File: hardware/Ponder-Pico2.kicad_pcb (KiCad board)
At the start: 2 copper layers, 40 x 50 mm, 136 parts, among them J1 USB_C_Receptacle_USB2.0, J10 2.54 SKT, J11 2.54 HDR, J12 1.27 HDR, J13 1.27 HDR, J14 1.27 HDR, J15 1.27 HDR, J2 2.54 HDR, J3 2.54 HDR, J4 2.54 HDR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

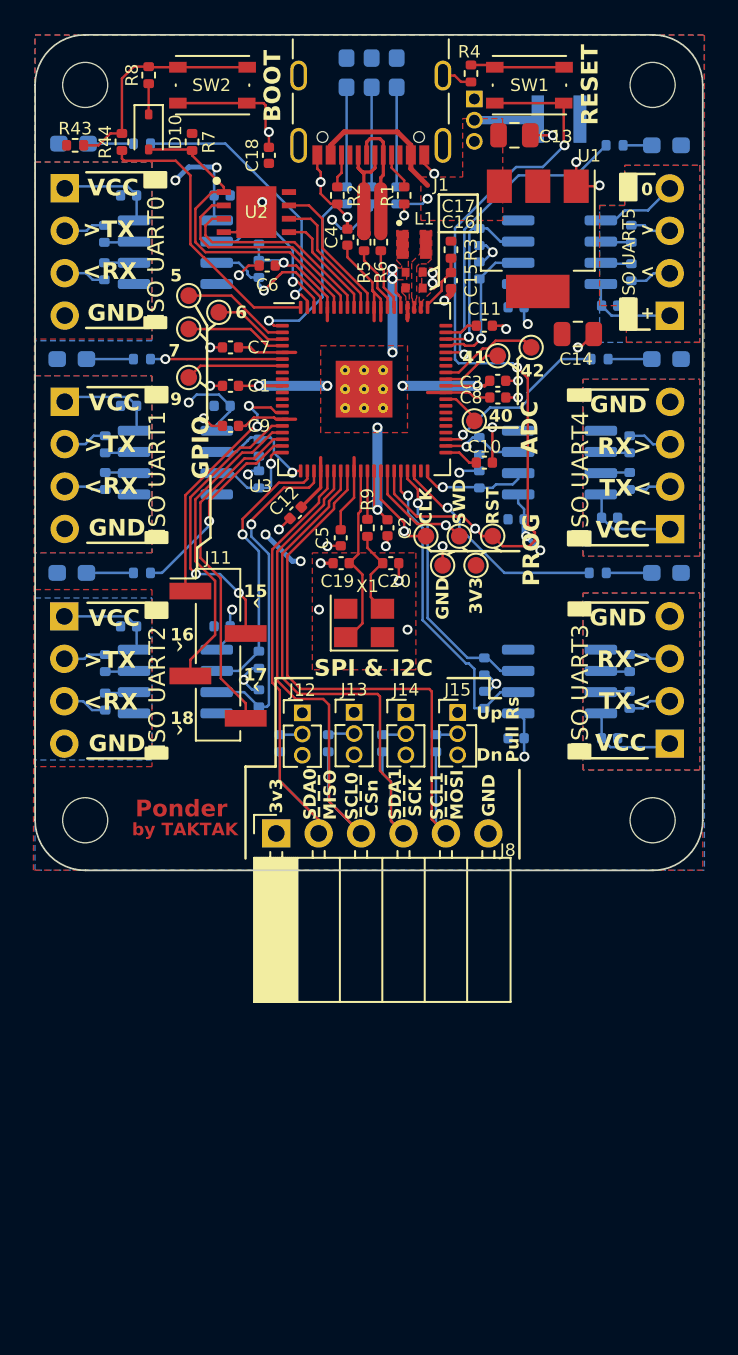
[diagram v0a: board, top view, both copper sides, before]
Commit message: Adding start of Pico 2 variant for Ponder
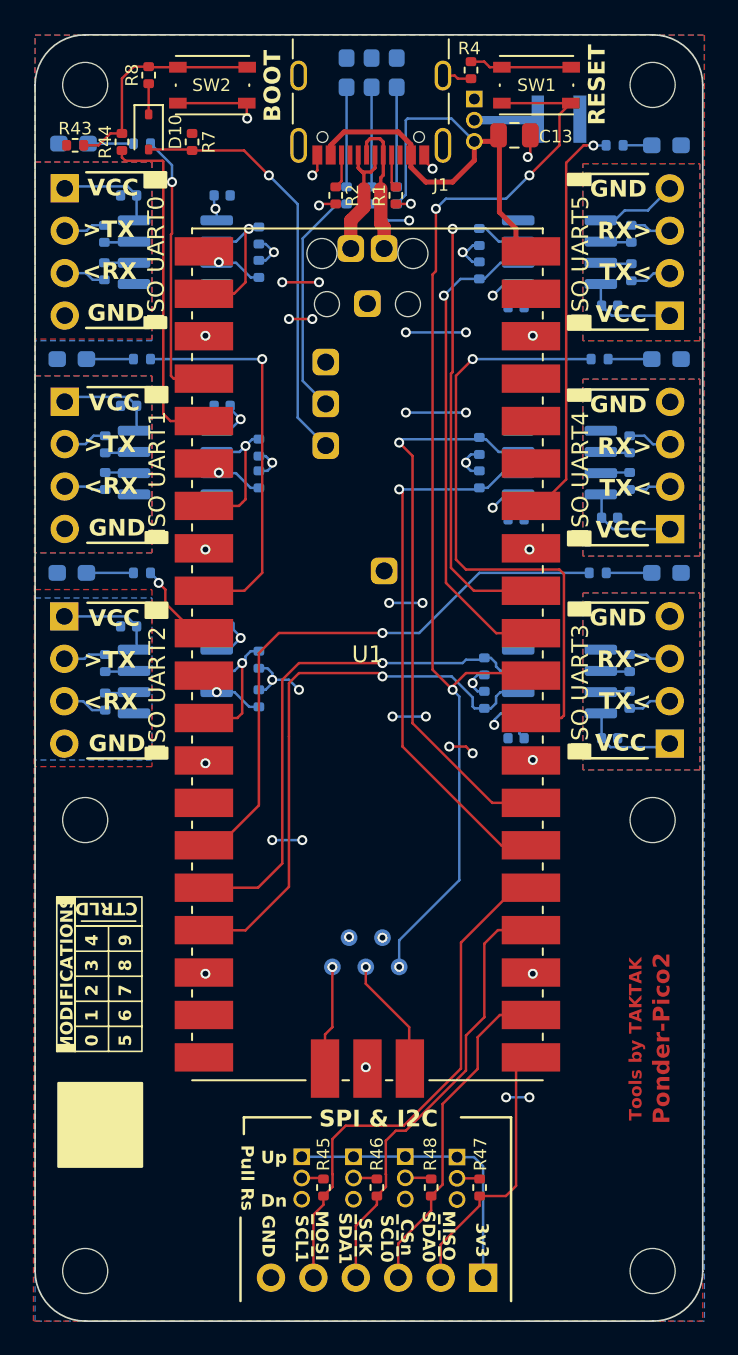
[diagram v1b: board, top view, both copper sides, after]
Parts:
- removed C1, C10, C11, C12, C18, C3, C4, C5, C6, C7, C8, C9: 100n, Capacitor_SMD:C_0402_1005Metric
- removed C14: 10u, Capacitor_SMD:C_0805_2012Metric
- removed C15, C2: 4.7u, Capacitor_SMD:C_0402_1005Metric
- removed C16, C17: 4.7u, Ponder:C_0402_1005Metric_small_pads
- removed C19, C20: 15p, Capacitor_SMD:C_0402_1005Metric
- removed J11: 2.54 HDR, Connector_PinHeader_2.54mm:PinHeader_1x04_P2.54mm_Vertical_SMD_Pin1Left
- removed L1: 3.3u, Ponder:L_pol_2016
- removed R3: 33, Resistor_SMD:R_0402_1005Metric
- removed R5, R6: 27, Resistor_SMD:R_0402_1005Metric
- removed R9: 1k, Resistor_SMD:R_0402_1005Metric
- removed TP10, TP11, TP12, TP6, TP7, TP8, TP9: TestPoint, TestPoint:TestPoint_Pad_D1.0mm
- removed U2: W25Q64JVXGIQ_TR, Ponder:SON80P400X400X50-9N
- removed U3: RP2350_80QFN, Ponder:RP2350-QFN-80-1EP_10x10_P0.4mm_EP3.4x3.4mm_ThermalVias
- removed X1: ABM8-272-T3, Crystal:Crystal_SMD_3225-4Pin_3.2x2.5mm
- added H5: MountingHole, MountingHole:MountingHole_2.7mm_M2.5, F.Cu at (123.6, 147.0)
- added H6: MountingHole, MountingHole:MountingHole_2.7mm_M2.5, F.Cu at (157.6, 147.0)
- G1, R45, R46, R47, R48: moved to F.Cu
- J12, J13, J14, J15, J8, TP1, TP2, TP3, TP4, TP5: moved to B.Cu
- U1: value NCP1117-3.3_SOT223 -> ~; footprint Package_TO_SOT_SMD:SOT-223-3_TabPin2 -> Ponder:RaspberryPi-Pico-SMD-TP
- moved U1 54.5 mm to (130.0, 135.6), turned to 0 degrees
- moved J8 29.3 mm to (147.4, 147.4)
- moved R47 29.2 mm to (147.2, 142.0)
- moved J15 28.2 mm to (136.6, 140.2), turned to 180 degrees
- moved J12 28.2 mm to (145.9, 140.2), turned to 180 degrees
- moved R45 27.4 mm to (137.9, 142.0)
- moved R48 27.3 mm to (144.3, 142.0)
- moved G1 26.9 mm to (125.0, 129.2), turned to 90 degrees
- moved J14 26.8 mm to (139.7, 140.2), turned to 180 degrees
- moved J13 26.8 mm to (142.8, 140.2), turned to 180 degrees
- moved R46 26.6 mm to (141.1, 142.0)
- moved TP1 26.4 mm to (138.4, 128.8)
- moved TP2 26.4 mm to (140.4, 128.8)
- moved TP5 26.4 mm to (142.4, 128.8)
- moved TP3 23.0 mm to (139.4, 127.0)
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- renumbered R25 to locked
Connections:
- D10 pad 2: /QSPI_SS -> /BOOTSEL
- J8 pad 2: /RP_SPI1-MISO_I2C0-SDA -> /RP_SPI0-MISO_I2C0-SDA
- J8 pad 3: /RP_SPI1-CSn_I2C0-SCL -> /RP_SPI0-CSn_I2C0-SCL
- J8 pad 4: /RP_SPI1-SCK_I2C1-SDA -> /RP_SPI0-SCK_I2C1-SDA
- J8 pad 5: /RP_SPI1-MOSI_I2C1-SCL -> /RP_SPI0-MOSI_I2C1-SCL
- R45 pad 2: /RP_SPI1-MOSI_I2C1-SCL -> /RP_SPI0-MOSI_I2C1-SCL
- R46 pad 2: /RP_SPI1-SCK_I2C1-SDA -> /RP_SPI0-SCK_I2C1-SDA
- R47 pad 2: /RP_SPI1-MISO_I2C0-SDA -> /RP_SPI0-MISO_I2C0-SDA
- R48 pad 2: /RP_SPI1-CSn_I2C0-SCL -> /RP_SPI0-CSn_I2C0-SCL
- R7 pad 2: /QSPI_SS -> /BOOTSEL
- U1 pad 1: GND -> /RP_UART0_TX
- U1 pad 2: +3V3 -> /RP_UART0_RX
- U1 pad 3: VBUS -> GND
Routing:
- net /RP_SPI1-MOSI_I2C1-SCL: track 36.8 -> 0.00 mm
- net /RP_SPI1-SCK_I2C1-SDA: track 34.3 -> 0.00 mm
- net /RP_SPI1-CSn_I2C0-SCL: track 31.9 -> 0.00 mm
- net /RP_SPI0-MOSI_I2C1-SCL: track 0.00 -> 30.4 mm
- net /RP_SPI1-MISO_I2C0-SDA: track 30.1 -> 0.00 mm
- net +1V1: track 29.7 -> 0.00 mm, vias 9 -> 0
- net /RP_UART4_TX: track 5.04 -> 32.9 mm
- net /RP_UART4_LED: track 11.1 -> 37.7 mm
- net /RP_SPI0-SCK_I2C1-SDA: track 0.00 -> 25.8 mm
- net /RP_UART4_RX: track 6.63 -> 32.2 mm
- net /BOOTSEL: track 0.00 -> 25.4 mm, vias 0 -> 1
- net VBUS: track 11.0 -> 32.1 mm, vias 1 -> 0
- net /RP_UART3_LED: track 13.6 -> 34.3 mm
- net /GPIO18: track 20.5 -> 0.00 mm
- net /QSPI_SS: track 20.3 -> 0.00 mm
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- removed copper zone on F.Cu, net +1V1
- removed copper zone on F.Cu, net /VREG_LX
- removed copper zone on F.Cu, net GND
- removed copper zone on F.Cu, net VBUS
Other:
- board size 40 x 50 mm -> 40 x 77 mm
- board text added: "Ponder-Pico2"
- board text added: "TP1"
- board text added: "TP2"
- board text added: "TP3"
- board text added: "TP4"
- board text added: "TP5"
- board text added: "TP6"
- board text added: "TP7"
- board text added: "Tools by TAKTAK"
- board text removed: "15"
- board text removed: "16"
- board text removed: "17"
- board text removed: "18"
- board text removed: "40"
- board text removed: "41"
- board text removed: "42"
- board text removed: "5"
- board text removed: "6"
- board text removed: "7"
- board text removed: "9"
- board text removed: "ADC"
- board text removed: "GPIO"
- board text removed: "Ponder"
- board text removed: "^"
- board text removed: "by TAKTAK"

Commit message: Modifying Pico footprint for USB holes to match DS
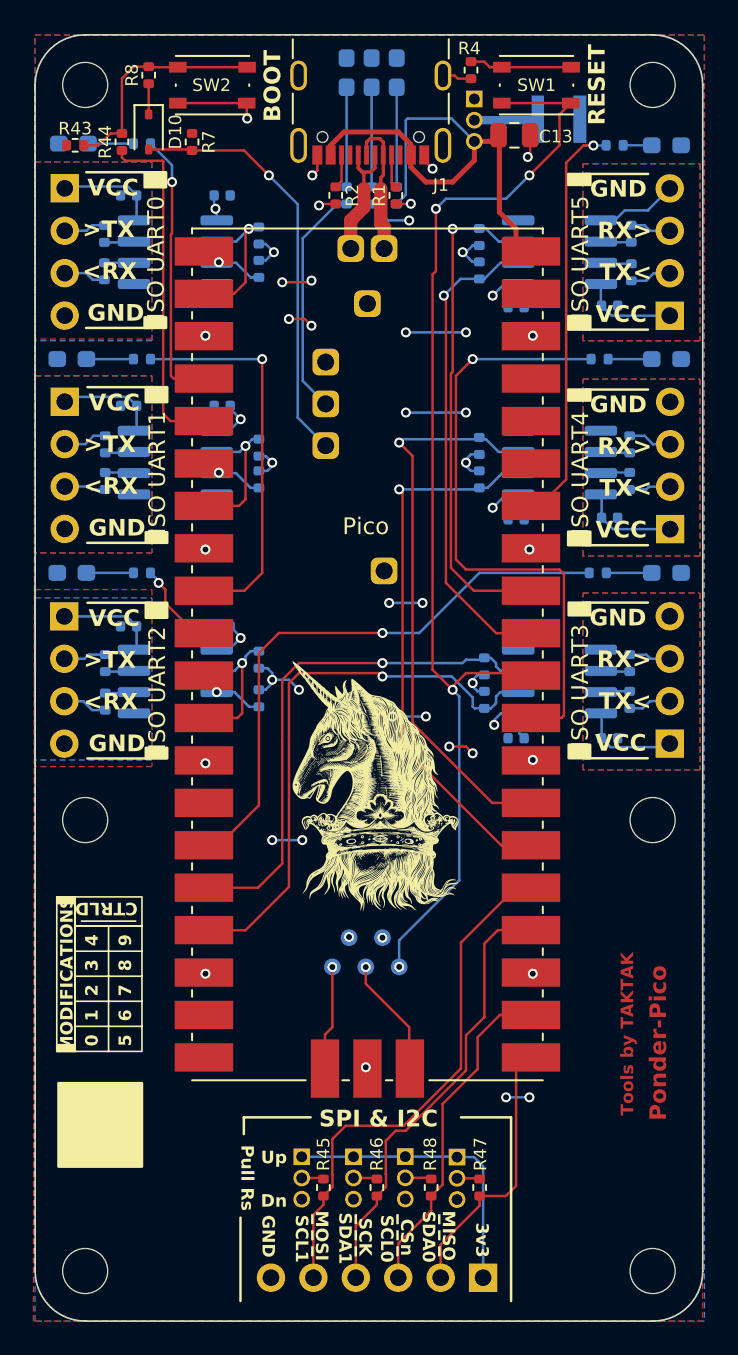
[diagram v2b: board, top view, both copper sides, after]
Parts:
- added G***: LOGO, Ponder:Crest-10mm, F.Cu at (141.0, 118.0)
- moved G2 17.9 mm to (130.0, 127.0)
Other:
- board text added: "Pico"
- board text added: "Ponder-Pico"
- board text removed: "Ponder-Pico2"
